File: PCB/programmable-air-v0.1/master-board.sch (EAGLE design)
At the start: 14 parts, among them J1 POWER_JACKTOE, Q1 600mA/40V, Q2 600mA/40V

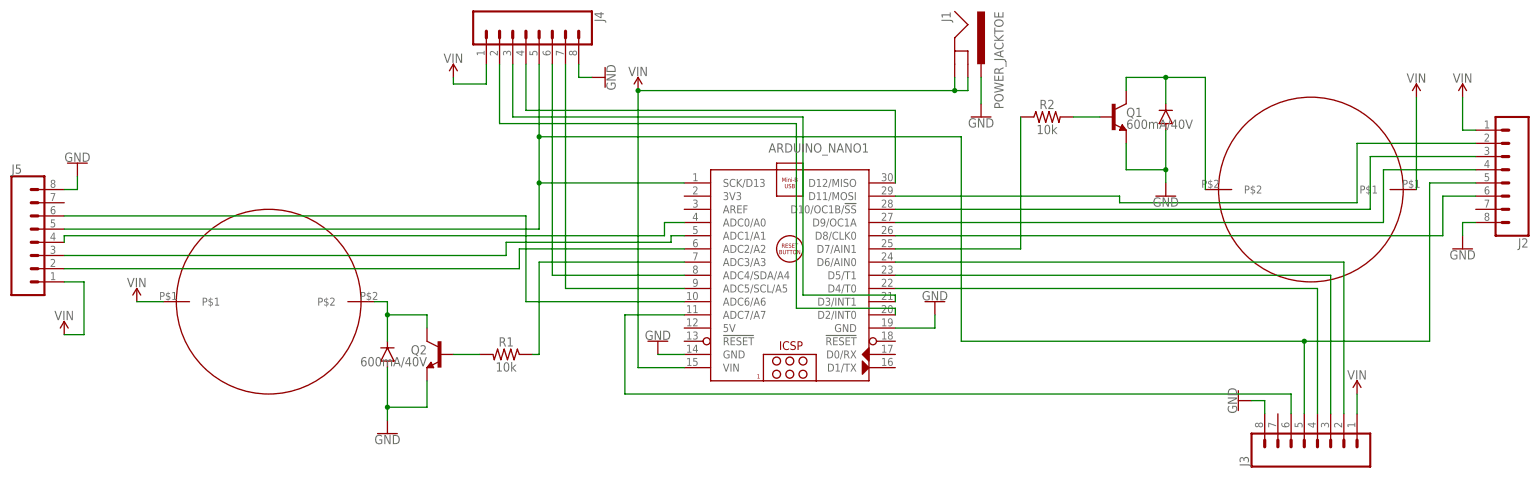
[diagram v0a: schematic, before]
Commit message: Started work on slave PCB. Made changes to master pcb after testing
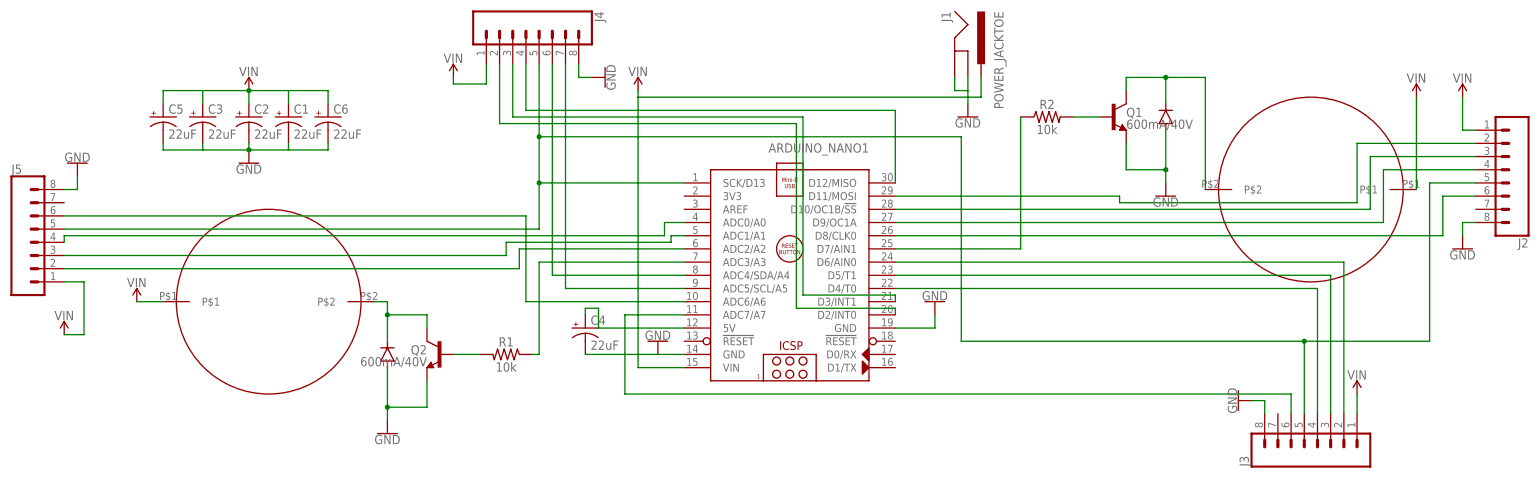
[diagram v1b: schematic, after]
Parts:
- added C1, C2, C3, C4, C5, C6: 22uF, SparkFun-Capacitors:22UF-POLAR-PANASONIC_C-35V-20%
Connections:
- new net N$20: ARDUINO_NANO1.5V, C4.+
- net GND: now also C1.-, C2.-, C3.-, C4.-, C5.-, C6.-, J1.GND, J1.GNDBREAK; no longer J1.PWR
- net VIN: now also C1.+, C2.+, C3.+, C5.+, C6.+, J1.PWR; no longer J1.GND, J1.GNDBREAK
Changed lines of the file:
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@@
 <part name="SUPPLY6" library="SparkFun-PowerSymbols" deviceset="VIN" device=""/>
 <part name="SUPPLY7" library="SparkFun-PowerSymbols" deviceset="VIN" device=""/>
+<part name="C1" library="SparkFun-Capacitors" deviceset="22UF-POLAR" device="-PANASONIC_C-35V-20%" value="22uF"/>
+<part name="C2" library="SparkFun-Capacitors" deviceset="22UF-POLAR" device="-PANASONIC_C-35V-20%" value="22uF"/>
+<part name="C3" library="SparkFun-Capacitors" deviceset="22UF-POLAR" device="-PANASONIC_C-35V-20%" value="22uF"/>
+<part name="GND10" library="SparkFun-PowerSymbols" deviceset="GND" device=""/>
+<part name="SUPPLY8" library="SparkFun-PowerSymbols" deviceset="VIN" device=""/>
+<part name="C4" library="SparkFun-Capacitors" deviceset="22UF-POLAR" device="-PANASONIC_C-35V-20%" value="22uF"/>
+<part name="C5" library="SparkFun-Capacitors" deviceset="22UF-POLAR" device="-PANASONIC_C-35V-20%" value="22uF"/>
+<part name="C6" library="SparkFun-Capacitors" deviceset="22UF-POLAR" device="-PANASONIC_C-35V-20%" value="22uF"/>
 </parts>
 <sheets>
@@
 <instance part="GND7" gate="1" x="85.09" y="-22.86" rot="R270"/>
 <instance part="GND8" gate="1" x="-138.43" y="22.86" rot="R180"/>
-<instance part="GND9" gate="1" x="35.56" y="31.75"/>
+<instance part="GND9" gate="1" x="33.02" y="31.75"/>
 <instance part="SUPPLY1" gate="G$1" x="119.38" y="35.56"/>
 <instance part="SUPPLY2" gate="G$1" x="-30.48" y="36.83"/>
@@
 <instance part="SUPPLY6" gate="G$1" x="128.27" y="35.56"/>
 <instance part="SUPPLY7" gate="G$1" x="-127" y="-3.81"/>
+<instance part="C1" gate="G$1" x="-97.79" y="31.75"/>
+<instance part="C2" gate="G$1" x="-105.41" y="31.75"/>
+<instance part="C3" gate="G$1" x="-114.3" y="31.75"/>
+<instance part="GND10" gate="1" x="-105.41" y="22.86"/>
+<instance part="SUPPLY8" gate="G$1" x="-105.41" y="36.83"/>
+<instance part="C4" gate="G$1" x="-40.64" y="-8.89"/>
+<instance part="C5" gate="G$1" x="-121.92" y="31.75"/>
+<instance part="C6" gate="G$1" x="-90.17" y="31.75"/>
 </instances>
 <busses>
@@
 <pinref part="ARDUINO_NANO1" gate="G$1" pin="GND@2"/>
 <wire x1="-21.59" y1="-13.97" x2="-26.67" y2="-13.97" width="0.1524" layer="91"/>
+<pinref part="C4" gate="G$1" pin="-"/>
+<wire x1="-40.64" y1="-13.97" x2="-26.67" y2="-13.97" width="0.1524" layer="91"/>
 </segment>
 <segment>
@@
 </segment>
 <segment>
-<pinref part="J1" gate="G$1" pin="PWR"/>
-<wire x1="35.56" y1="39.37" x2="35.56" y2="34.29" width="0.1524" layer="91"/>
+<pinref part="J1" gate="G$1" pin="GNDBREAK"/>
+<wire x1="33.02" y1="39.37" x2="33.02" y2="36.83" width="0.1524" layer="91"/>
+<wire x1="33.02" y1="36.83" x2="30.48" y2="36.83" width="0.1524" layer="91"/>
+<pinref part="J1" gate="G$1" pin="GND"/>
+<wire x1="30.48" y1="39.37" x2="30.48" y2="36.83" width="0.1524" layer="91"/>
 <pinref part="GND9" gate="1" pin="GND"/>
+<wire x1="33.02" y1="34.29" x2="33.02" y2="36.83" width="0.1524" layer="91"/>
+</segment>
+<segment>
+<pinref part="C3" gate="G$1" pin="-"/>
+<wire x1="-114.3" y1="26.67" x2="-114.3" y2="25.4" width="0.1524" layer="91"/>
+<wire x1="-114.3" y1="25.4" x2="-105.41" y2="25.4" width="0.1524" layer="91"/>
+<pinref part="C2" gate="G$1" pin="-"/>
+<wire x1="-105.41" y1="25.4" x2="-105.41" y2="26.67" width="0.1524" layer="91"/>
+<wire x1="-105.41" y1="25.4" x2="-97.79" y2="25.4" width="0.1524" layer="91"/>
+<pinref part="C1" gate="G$1" pin="-"/>
+<wire x1="-97.79" y1="25.4" x2="-97.79" y2="26.67" width="0.1524" layer="91"/>
+<pinref part="GND10" gate="1" pin="GND"/>
+<junction x="-105.41" y="25.4"/>
+<pinref part="C5" gate="G$1" pin="-"/>
+<wire x1="-114.3" y1="25.4" x2="-121.92" y2="25.4" width="0.1524" layer="91"/>
+<wire x1="-121.92" y1="25.4" x2="-121.92" y2="26.67" width="0.1524" layer="91"/>
+<pinref part="C6" gate="G$1" pin="-"/>
+<wire x1="-90.17" y1="26.67" x2="-90.17" y2="25.4" width="0.1524" layer="91"/>
+<wire x1="-90.17" y1="25.4" x2="-97.79" y2="25.4" width="0.1524" layer="91"/>
 </segment>
 </net>
@@
 <pinref part="ARDUINO_NANO1" gate="G$1" pin="VIN"/>
 <wire x1="-21.59" y1="-16.51" x2="-30.48" y2="-16.51" width="0.1524" layer="91"/>
-<pinref part="J1" gate="G$1" pin="GNDBREAK"/>
-<wire x1="33.02" y1="39.37" x2="33.02" y2="36.83" width="0.1524" layer="91"/>
-<wire x1="33.02" y1="36.83" x2="30.48" y2="36.83" width="0.1524" layer="91"/>
-<pinref part="J1" gate="G$1" pin="GND"/>
-<wire x1="30.48" y1="39.37" x2="30.48" y2="36.83" width="0.1524" layer="91"/>
-<wire x1="-30.48" y1="-16.51" x2="-30.48" y2="36.83" width="0.1524" layer="91"/>
-<wire x1="-30.48" y1="36.83" x2="30.48" y2="36.83" width="0.1524" layer="91"/>
+<wire x1="-30.48" y1="-16.51" x2="-30.48" y2="35.56" width="0.1524" layer="91"/>
 <pinref part="SUPPLY2" gate="G$1" pin="VIN"/>
-<junction x="-30.48" y="36.83"/>
-<junction x="30.48" y="36.83"/>
+<pinref part="J1" gate="G$1" pin="PWR"/>
+<wire x1="-30.48" y1="35.56" x2="-30.48" y2="36.83" width="0.1524" layer="91"/>
+<wire x1="35.56" y1="39.37" x2="35.56" y2="35.56" width="0.1524" layer="91"/>
+<wire x1="35.56" y1="35.56" x2="-30.48" y2="35.56" width="0.1524" layer="91"/>
 </segment>
 <segment>
@@
 <pinref part="SUPPLY5" gate="G$1" pin="VIN"/>
 <wire x1="107.95" y1="-25.4" x2="107.95" y2="-21.59" width="0.1524" layer="91"/>
+</segment>
+<segment>
+<pinref part="C1" gate="G$1" pin="+"/>
+<wire x1="-97.79" y1="34.29" x2="-97.79" y2="36.83" width="0.1524" layer="91"/>
+<wire x1="-97.79" y1="36.83" x2="-105.41" y2="36.83" width="0.1524" layer="91"/>
+<pinref part="C2" gate="G$1" pin="+"/>
+<wire x1="-105.41" y1="36.83" x2="-105.41" y2="34.29" width="0.1524" layer="91"/>
+<pinref part="C3" gate="G$1" pin="+"/>
+<wire x1="-114.3" y1="36.83" x2="-114.3" y2="34.29" width="0.1524" layer="91"/>
+<pinref part="SUPPLY8" gate="G$1" pin="VIN"/>
+<junction x="-105.41" y="36.83"/>
+<pinref part="C5" gate="G$1" pin="+"/>
+<wire x1="-121.92" y1="34.29" x2="-121.92" y2="36.83" width="0.1524" layer="91"/>
+<wire x1="-121.92" y1="36.83" x2="-114.3" y2="36.83" width="0.1524" layer="91"/>
+<wire x1="-114.3" y1="36.83" x2="-105.41" y2="36.83" width="0.1524" layer="91"/>
+<pinref part="C6" gate="G$1" pin="+"/>
+<wire x1="-97.79" y1="36.83" x2="-90.17" y2="36.83" width="0.1524" layer="91"/>
+<wire x1="-90.17" y1="36.83" x2="-90.17" y2="34.29" width="0.1524" layer="91"/>
 </segment>
 </net>
@@
 </segment>
 </net>
+<net name="N$20" class="0">
+<segment>
+<pinref part="ARDUINO_NANO1" gate="G$1" pin="5V"/>
+<wire x1="-21.59" y1="-8.89" x2="-38.1" y2="-8.89" width="0.1524" layer="91"/>
+<wire x1="-38.1" y1="-8.89" x2="-38.1" y2="-5.08" width="0.1524" layer="91"/>
+<wire x1="-38.1" y1="-5.08" x2="-40.64" y2="-5.08" width="0.1524" layer="91"/>
+<pinref part="C4" gate="G$1" pin="+"/>
+<wire x1="-40.64" y1="-5.08" x2="-40.64" y2="-6.35" width="0.1524" layer="91"/>
+</segment>
+</net>

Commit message: PCB v0.11 master ready for production
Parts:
- removed Q1, Q2: 600mA/40V, SparkFun-DiscreteSemi:TRANS_NPN-MMBT2222AL
- added U$5, U$6: TIP120-TO220, programmable-air-components:TIP120-TO220
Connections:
- net GND: now also U$5.E, U$6.E; no longer Q1.E, Q2.E, U$3.P$2, U$4.P$2
- net N$2: now also U$6.B; no longer Q2.B
- net N$5: now also U$3.P$2, U$6.C; no longer Q2.C, U$3.P$1
- net N$6: now also U$4.P$2, U$5.C; no longer Q1.C, U$4.P$1
- net N$7: now also U$5.B; no longer Q1.B
- net VIN: now also U$3.P$1, U$4.P$1
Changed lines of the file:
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@@
 <part name="U$1" library="programmable-air-components" deviceset="AIYIMA-PUMP-A5F083" device=""/>
 <part name="U$2" library="programmable-air-components" deviceset="AIYIMA-PUMP-A5F083" device=""/>
-<part name="Q2" library="SparkFun-DiscreteSemi" deviceset="TRANS_NPN" device="-MMBT2222AL" value="600mA/40V"/>
-<part name="Q1" library="SparkFun-DiscreteSemi" deviceset="TRANS_NPN" device="-MMBT2222AL" value="600mA/40V"/>
-<part name="U$3" library="programmable-air-components" deviceset="IN4148" device=""/>
-<part name="U$4" library="programmable-air-components" deviceset="IN4148" device=""/>
 <part name="R1" library="SparkFun-Resistors" deviceset="10KOHM" device="-0603-1/10W-1%" value="10k"/>
 <part name="R2" library="SparkFun-Resistors" deviceset="10KOHM" device="-0603-1/10W-1%" value="10k"/>
@@
 <part name="C5" library="SparkFun-Capacitors" deviceset="22UF-POLAR" device="-PANASONIC_C-35V-20%" value="22uF"/>
 <part name="C6" library="SparkFun-Capacitors" deviceset="22UF-POLAR" device="-PANASONIC_C-35V-20%" value="22uF"/>
+<part name="U$5" library="programmable-air-components" deviceset="TIP120-TO220" device=""/>
+<part name="U$6" library="programmable-air-components" deviceset="TIP120-TO220" device=""/>
+<part name="U$3" library="programmable-air-components" deviceset="IN4148" device=""/>
+<part name="U$4" library="programmable-air-components" deviceset="IN4148" device=""/>
 </parts>
 <sheets>
@@
 <instance part="U$1" gate="G$1" x="-101.6" y="-3.81" rot="MR0"/>
 <instance part="U$2" gate="G$1" x="99.06" y="17.78"/>
-<instance part="Q2" gate="G$1" x="-68.58" y="-13.97" rot="MR0"/>
-<instance part="Q1" gate="G$1" x="60.96" y="31.75"/>
-<instance part="U$3" gate="G$1" x="-78.74" y="-13.97" rot="MR90"/>
-<instance part="U$4" gate="G$1" x="71.12" y="31.75" rot="R90"/>
 <instance part="R1" gate="G$1" x="-55.88" y="-13.97" rot="MR0"/>
 <instance part="R2" gate="G$1" x="48.26" y="31.75"/>
@@
 <instance part="C5" gate="G$1" x="-121.92" y="31.75"/>
 <instance part="C6" gate="G$1" x="-90.17" y="31.75"/>
+<instance part="U$5" gate="G$1" x="60.96" y="31.75"/>
+<instance part="U$6" gate="G$1" x="-68.58" y="-13.97" rot="MR0"/>
+<instance part="U$3" gate="G$1" x="-102.87" y="-27.94" rot="R180"/>
+<instance part="U$4" gate="G$1" x="97.79" y="39.37"/>
 </instances>
 <busses>
@@
 <net name="N$2" class="0">
 <segment>
-<pinref part="Q2" gate="G$1" pin="B"/>
 <pinref part="R1" gate="G$1" pin="2"/>
 <wire x1="-66.04" y1="-13.97" x2="-60.96" y2="-13.97" width="0.1524" layer="91"/>
+<pinref part="U$6" gate="G$1" pin="B"/>
 </segment>
 </net>
 <net name="N$5" class="0">
 <segment>
-<pinref part="U$3" gate="G$1" pin="P$1"/>
-<wire x1="-78.74" y1="-11.43" x2="-78.74" y2="-6.35" width="0.1524" layer="91"/>
 <wire x1="-78.74" y1="-6.35" x2="-71.12" y2="-6.35" width="0.1524" layer="91"/>
-<pinref part="Q2" gate="G$1" pin="C"/>
 <wire x1="-71.12" y1="-6.35" x2="-71.12" y2="-8.89" width="0.1524" layer="91"/>
 <pinref part="U$1" gate="G$1" pin="P$2"/>
 <wire x1="-78.74" y1="-6.35" x2="-78.74" y2="-3.81" width="0.1524" layer="91"/>
 <wire x1="-78.74" y1="-3.81" x2="-81.28" y2="-3.81" width="0.1524" layer="91"/>
-<junction x="-78.74" y="-6.35"/>
+<pinref part="U$6" gate="G$1" pin="C"/>
+<pinref part="U$3" gate="G$1" pin="P$2"/>
+<wire x1="-100.33" y1="-27.94" x2="-81.28" y2="-27.94" width="0.1524" layer="91"/>
+<wire x1="-81.28" y1="-27.94" x2="-81.28" y2="-3.81" width="0.1524" layer="91"/>
 </segment>
 </net>
@@
 <pinref part="U$2" gate="G$1" pin="P$2"/>
 <wire x1="78.74" y1="17.78" x2="78.74" y2="39.37" width="0.1524" layer="91"/>
-<pinref part="U$4" gate="G$1" pin="P$1"/>
-<wire x1="78.74" y1="39.37" x2="71.12" y2="39.37" width="0.1524" layer="91"/>
-<pinref part="Q1" gate="G$1" pin="C"/>
-<wire x1="71.12" y1="39.37" x2="71.12" y2="34.29" width="0.1524" layer="91"/>
-<wire x1="71.12" y1="39.37" x2="63.5" y2="39.37" width="0.1524" layer="91"/>
+<wire x1="78.74" y1="39.37" x2="63.5" y2="39.37" width="0.1524" layer="91"/>
 <wire x1="63.5" y1="39.37" x2="63.5" y2="36.83" width="0.1524" layer="91"/>
-<junction x="71.12" y="39.37"/>
+<pinref part="U$5" gate="G$1" pin="C"/>
+<pinref part="U$4" gate="G$1" pin="P$2"/>
+<wire x1="78.74" y1="39.37" x2="95.25" y2="39.37" width="0.1524" layer="91"/>
 </segment>
 </net>
 <net name="N$7" class="0">
 <segment>
-<pinref part="Q1" gate="G$1" pin="B"/>
 <pinref part="R2" gate="G$1" pin="2"/>
 <wire x1="58.42" y1="31.75" x2="53.34" y2="31.75" width="0.1524" layer="91"/>
+<pinref part="U$5" gate="G$1" pin="B"/>
 </segment>
 </net>
@@
 </segment>
 <segment>
-<pinref part="Q2" gate="G$1" pin="E"/>
 <wire x1="-71.12" y1="-24.13" x2="-71.12" y2="-19.05" width="0.1524" layer="91"/>
-<pinref part="U$3" gate="G$1" pin="P$2"/>
 <wire x1="-71.12" y1="-24.13" x2="-78.74" y2="-24.13" width="0.1524" layer="91"/>
-<wire x1="-78.74" y1="-24.13" x2="-78.74" y2="-16.51" width="0.1524" layer="91"/>
 <pinref part="GND1" gate="1" pin="GND"/>
 <wire x1="-78.74" y1="-26.67" x2="-78.74" y2="-24.13" width="0.1524" layer="91"/>
-<junction x="-78.74" y="-24.13"/>
-</segment>
-<segment>
-<pinref part="Q1" gate="G$1" pin="E"/>
+<pinref part="U$6" gate="G$1" pin="E"/>
+</segment>
+<segment>
 <wire x1="63.5" y1="26.67" x2="63.5" y2="21.59" width="0.1524" layer="91"/>
 <wire x1="63.5" y1="21.59" x2="71.12" y2="21.59" width="0.1524" layer="91"/>
-<pinref part="U$4" gate="G$1" pin="P$2"/>
-<wire x1="71.12" y1="21.59" x2="71.12" y2="29.21" width="0.1524" layer="91"/>
 <pinref part="GND2" gate="1" pin="GND"/>
 <wire x1="71.12" y1="19.05" x2="71.12" y2="21.59" width="0.1524" layer="91"/>
-<junction x="71.12" y="21.59"/>
+<pinref part="U$5" gate="G$1" pin="E"/>
 </segment>
 <segment>
@@
 <pinref part="U$1" gate="G$1" pin="P$1"/>
 <pinref part="SUPPLY7" gate="G$1" pin="VIN"/>
-<wire x1="-121.92" y1="-3.81" x2="-127" y2="-3.81" width="0.1524" layer="91"/>
+<wire x1="-121.92" y1="-3.81" x2="-123.19" y2="-3.81" width="0.1524" layer="91"/>
+<wire x1="-123.19" y1="-3.81" x2="-127" y2="-3.81" width="0.1524" layer="91"/>
+<wire x1="-123.19" y1="-3.81" x2="-123.19" y2="-27.94" width="0.1524" layer="91"/>
+<pinref part="U$3" gate="G$1" pin="P$1"/>
+<wire x1="-123.19" y1="-27.94" x2="-105.41" y2="-27.94" width="0.1524" layer="91"/>
 </segment>
 <segment>
@@
 <pinref part="SUPPLY1" gate="G$1" pin="VIN"/>
 <pinref part="U$2" gate="G$1" pin="P$1"/>
-<wire x1="119.38" y1="35.56" x2="119.38" y2="17.78" width="0.1524" layer="91"/>
-</segment>
-<segment>
+<wire x1="119.38" y1="35.56" x2="119.38" y2="33.02" width="0.1524" layer="91"/>
+<wire x1="119.38" y1="33.02" x2="119.38" y2="17.78" width="0.1524" layer="91"/>
+<wire x1="100.33" y1="39.37" x2="116.84" y2="39.37" width="0.1524" layer="91"/>
+<wire x1="116.84" y1="39.37" x2="116.84" y2="33.02" width="0.1524" layer="91"/>
+<wire x1="116.84" y1="33.02" x2="119.38" y2="33.02" width="0.1524" layer="91"/>
+<pinref part="U$4" gate="G$1" pin="P$1"/>
+</segment>
+<segment>

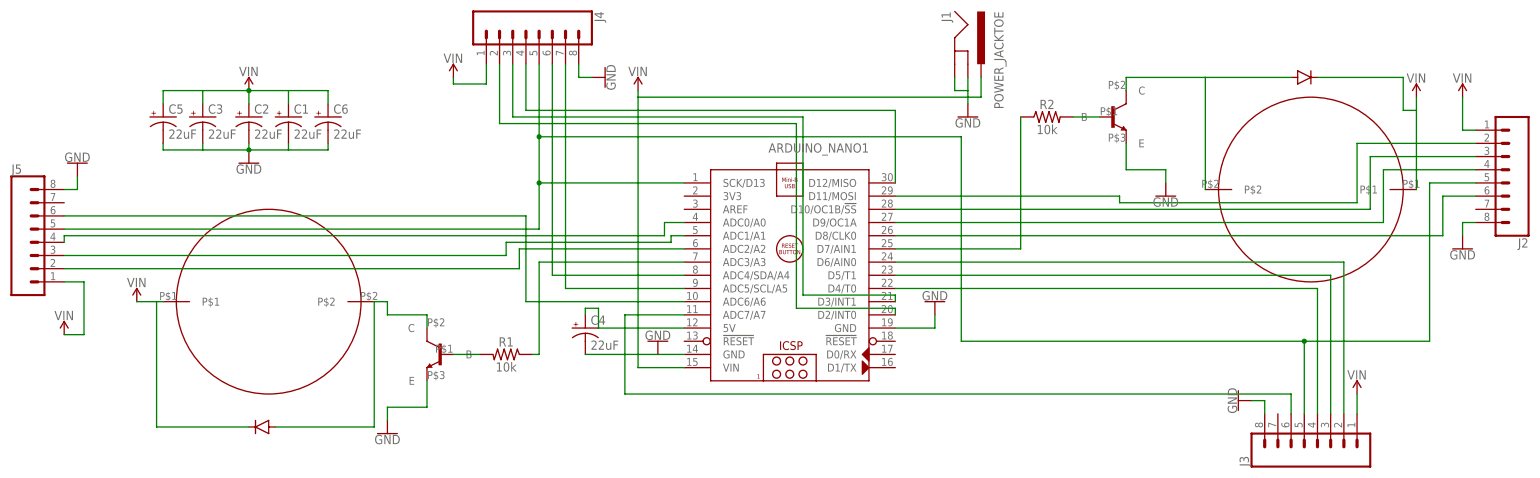
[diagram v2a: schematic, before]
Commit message: Forgot to add 5V input to slave boards
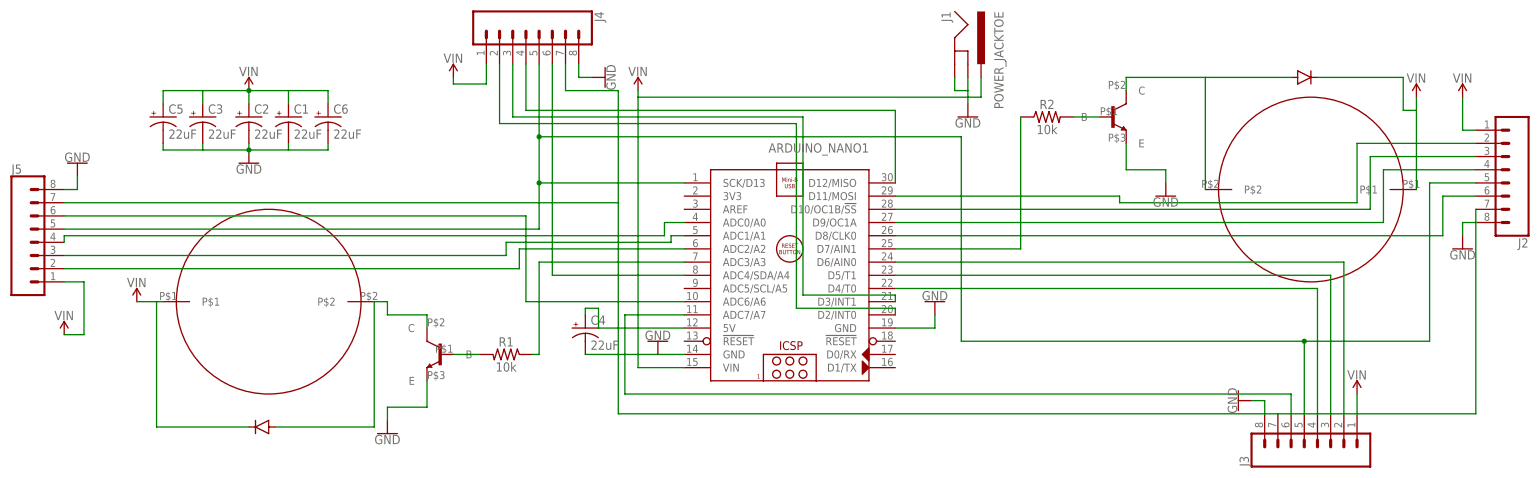
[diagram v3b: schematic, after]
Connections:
- removed net N$12: ARDUINO_NANO1.ADC5/SCL/A5, J4.7
- net N$20: now also J2.7, J3.7, J4.7, J5.7
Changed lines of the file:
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@@
-</segment>
-</net>
-<net name="N$12" class="0">
-<segment>
-<pinref part="ARDUINO_NANO1" gate="G$1" pin="ADC5/SCL/A5"/>
-<pinref part="J4" gate="G$1" pin="7"/>
-<wire x1="-21.59" y1="-1.27" x2="-44.45" y2="-1.27" width="0.1524" layer="91"/>
-<wire x1="-44.45" y1="-1.27" x2="-44.45" y2="41.91" width="0.1524" layer="91"/>
 </segment>
 </net>
@@
 <segment>
 <pinref part="ARDUINO_NANO1" gate="G$1" pin="5V"/>
-<wire x1="-21.59" y1="-8.89" x2="-38.1" y2="-8.89" width="0.1524" layer="91"/>
+<wire x1="-21.59" y1="-8.89" x2="-34.29" y2="-8.89" width="0.1524" layer="91"/>
+<wire x1="-34.29" y1="-8.89" x2="-38.1" y2="-8.89" width="0.1524" layer="91"/>
 <wire x1="-38.1" y1="-8.89" x2="-38.1" y2="-5.08" width="0.1524" layer="91"/>
 <wire x1="-38.1" y1="-5.08" x2="-40.64" y2="-5.08" width="0.1524" layer="91"/>
 <pinref part="C4" gate="G$1" pin="+"/>
 <wire x1="-40.64" y1="-5.08" x2="-40.64" y2="-6.35" width="0.1524" layer="91"/>
-</segment>
-</net>
+<pinref part="J5" gate="G$1" pin="7"/>
+<wire x1="-140.97" y1="15.24" x2="-34.29" y2="15.24" width="0.1524" layer="91"/>
+<wire x1="-34.29" y1="15.24" x2="-34.29" y2="-8.89" width="0.1524" layer="91"/>
+<pinref part="J4" gate="G$1" pin="7"/>
+<wire x1="-44.45" y1="41.91" x2="-44.45" y2="36.83" width="0.1524" layer="91"/>
+<wire x1="-44.45" y1="36.83" x2="-34.29" y2="36.83" width="0.1524" layer="91"/>
+<wire x1="-34.29" y1="36.83" x2="-34.29" y2="15.24" width="0.1524" layer="91"/>
+<wire x1="-34.29" y1="-8.89" x2="-34.29" y2="-25.4" width="0.1524" layer="91"/>
+<pinref part="J3" gate="G$1" pin="7"/>
+<wire x1="-34.29" y1="-25.4" x2="92.71" y2="-25.4" width="0.1524" layer="91"/>
+<pinref part="J2" gate="G$1" pin="7"/>
+<wire x1="130.81" y1="13.97" x2="130.81" y2="-25.4" width="0.1524" layer="91"/>
+<wire x1="130.81" y1="-25.4" x2="92.71" y2="-25.4" width="0.1524" layer="91"/>
+</segment>
+</net>
